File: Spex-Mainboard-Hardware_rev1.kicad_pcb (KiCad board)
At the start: 4 copper layers, 100 x 80 mm, 134 parts, among them K1 G5LE_1A4_DC3, K2 G5LE_1A4_DC3, P1 USB_OTG, P10 CONN_01X02, P11 CONN_01X02, P12 CONN_01X02, P13 CONN_01X02, P2 SWD Header, P3 CONN_01X04, P4 CONN_01X04, P5 CONN_01X04, P6 CONN_01X04, P7 CONN_01X02, P8 CONN_01X02, P9 CONN_01X02, Q1 2N7002K, Q101 MOS_N_numbered, Q104 MOS_N_numbered, Q105 Si3407DV, Q106 Q_PNP_BEC, Q2 2N7002K, Q3 BSS215PH6327, Q4 Si5468DC, Q5 Si5468DC, Q6 Si5468DC, SW1 SW_PUSH, U1 MKL04Z32VLC4, U10 LM4030, U105 TPS563200, U108 TPS563200, U11 MCP2551-I/SN, U12 ST1480ABDR, U13 SCHA4B0419, U14 AT45DB641E, U2 NUP2201MR6, U3 MK20DX256VLH7, U4 NUP2201MR6, U5 NUP2201MR6, U6 MMQA6V2T1G, U7 MCP9808T, U8 BME280, U9 LSM9DS1, Y1 Crystal

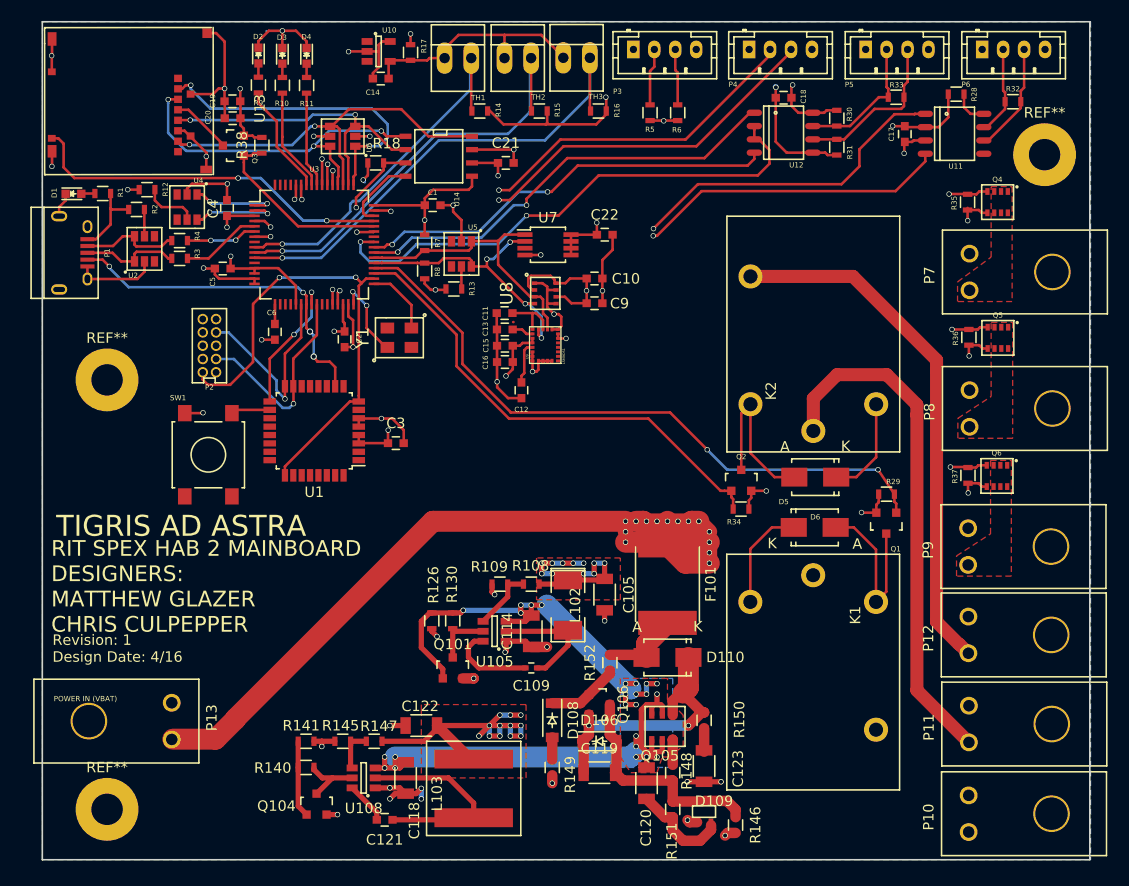
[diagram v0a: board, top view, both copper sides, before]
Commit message: rev 2 of hab board in progress
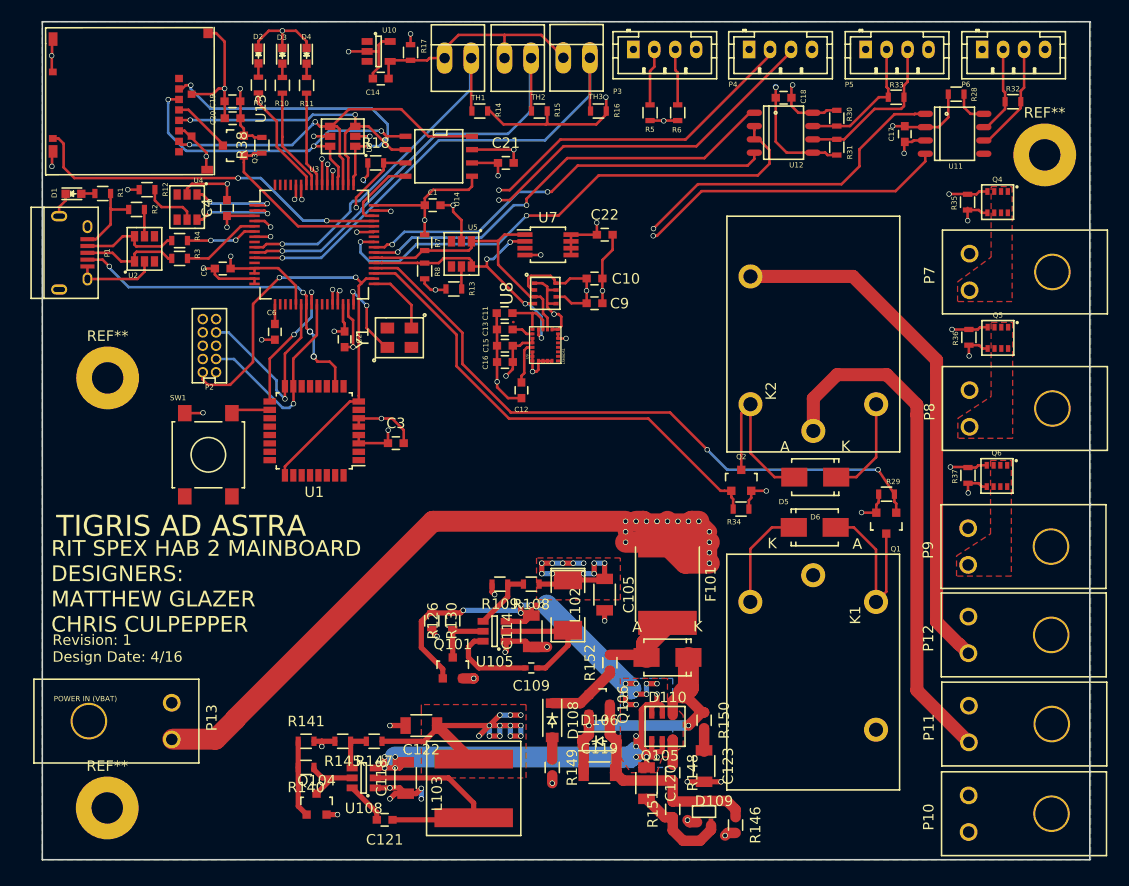
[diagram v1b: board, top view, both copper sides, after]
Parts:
- moved REF** 0.19 mm to (90.1, 84.8)
- moved REF** 0.14 mm to (90.0, 125.9)
- moved U13 0.10 mm to (100.0, 65.4)
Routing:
- net (no net): track 2.73 -> 0.07 mm
- net VBatt: track 107.1 -> 107.7 mm
